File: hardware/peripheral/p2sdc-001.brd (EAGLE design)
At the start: 91 x 90 mm, 72 parts, among them IC1 74LS06N, IC2 4066N, J1 MKR, J10 1-Wire, J2 GPIO, J3 Vcc, J4** RLY2, J5 SPI, J6 LED, J7 DIN5, J8 DIN5, J9 DIN5, K1 G5V1, Q1 220mA/50V/3.5Ω, Q2 220mA/50V/3.5Ω, T1 2SC1815, U1 DS18B20

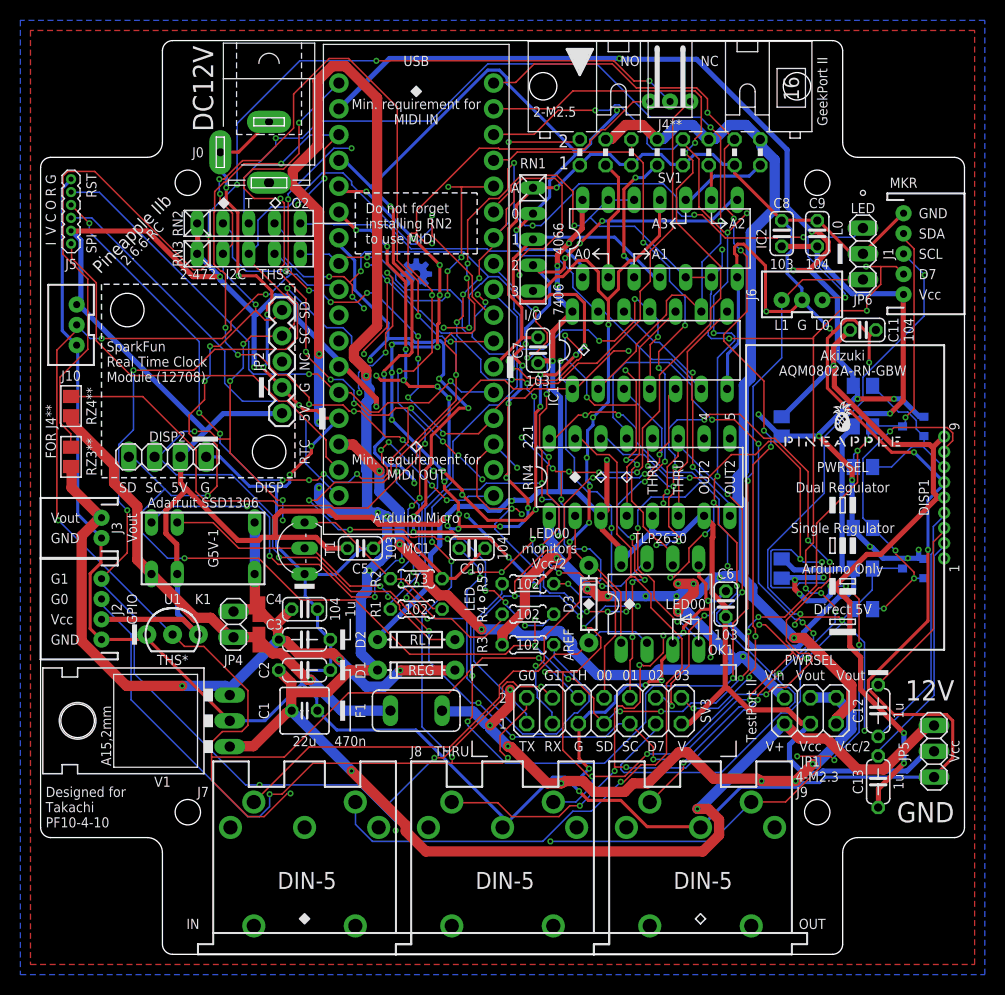
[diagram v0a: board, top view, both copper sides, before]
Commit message: Removed parts.
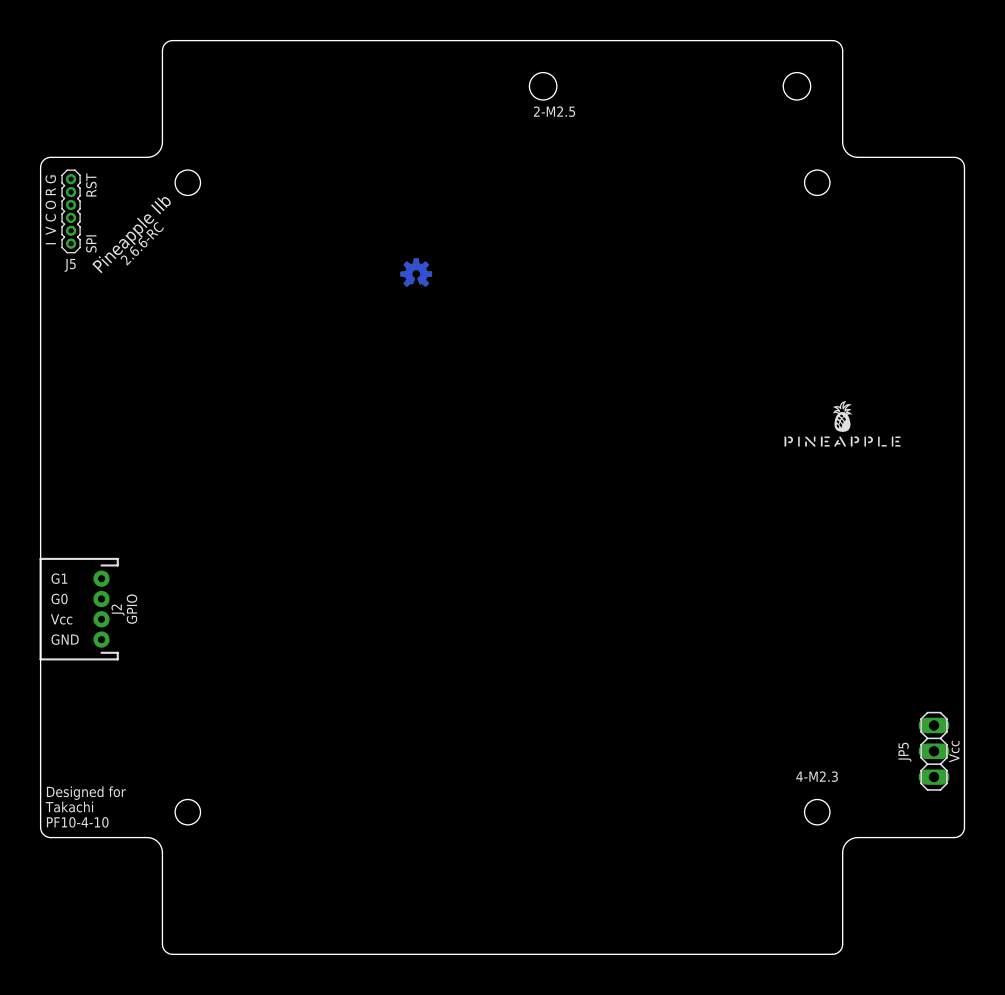
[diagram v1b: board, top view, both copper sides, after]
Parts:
- removed A, B: (no value), wirepad:SMD1,27-2,54
- removed C1: 22u, rcl:C025-050X050
- removed C10, C11, C4: 100n, rcl:C025-024X044
- removed C12, C13, C3: 1u, rcl:C050-024X044
- removed C2: 470n, rcl:C050-024X044
- removed C5, C6, C7, C8: 10n, resistor:C025-024X044
- removed C9: 100n, resistor:C025-024X044
- removed D1, D2, D3: (no value), SparkFun-DiscreteSemi:DIODE-1N4148
- removed DISP1: AQM0802A-RN-GBW, AQM0802A-RN-GBW:AQM0802A-RN-GBW-FOOTPRINT
- removed DISP2: MNTR, pinhead:1X04
- removed F1: 1.8A, fuse:TE5
- removed H1, H2: STAND-OFF, SparkFun-Hardware:STAND-OFF
- removed IC1: 74LS06N, 74xx-us:DIL14
- removed IC2: 4066N, 40xx:DIL14
- removed J0: (no value), con-jack:SPC4077
- removed J1: MKR, SparkFun-Connectors:JST-5-PTH
- removed J10: 1-Wire, SparkFun-Connectors:JST-3-PTH-VERT
- removed J3: Vcc, SparkFun-Connectors:JST-2-PTH
- removed J4**: RLY2, SparkFun-Connectors:JST-3-PTH-NS
- removed J6: LED, SparkFun-Connectors:JST-3-PTH-VERT
- removed J7, J8, J9: DIN5, SparkFun-Connectors:DIN5-RA-PTH
- removed JP1: PWRSEL, pinhead:2X03
- removed JP2: RTC, SparkFun-Connectors:1X05
- removed JP4: RLYJMP, pinhead:1X02
- removed JP6: LED, pinhead:1X03
- removed K1: G5V1, relay:G5V1
- removed MC1: ARDUINOMICRO, adafruit:ARDUINOMICRO
- removed OK1: HCPL2630, optocoupler:DIL08
- removed Q1, Q2: 220mA/50V/3.5Ω, SparkFun-DiscreteSemi:SOT23-3
- removed R1, R3, R4, R5: 1k, resistor:0204/5
- removed R101, R102, R103, R104: 10k, rcl:M2012
- removed R2: 47k, resistor:0204/5
- removed RN1: 10k, resistor-net:RN-5
- removed RN2, RN3: 4.7k, resistor-net:RN-5
- removed RN4: 220, resistor-dil:DIL16
- removed RZ1***, RZ2***, RZ3**, RZ4**, VCCBRIDGE***: Inf, rcl:M2012
- removed SV1: (no value), con-ml:ML16L
- removed SV3: Testport II, pinhead:2X07
- removed T1: 2SC1815, transistor:TO92-ECB
- removed U1: DS18B20, SparkFun-Sensors:TO-92-AMMO
- removed V1: 5V, v-reg:78XXL
- removed VDDBRIDGE: 0, rcl:M2012
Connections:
- removed net ANLG0: IC2.1, MC1.P$31, RN1.2
- removed net ANLG0R: IC2.2, SV1.3
- removed net ANLG1: IC2.4, MC1.P$30, RN1.3
- removed net ANLG1R: IC2.3, SV1.7
- removed net ANLG2: IC2.8, MC1.P$29, RN1.4
- removed net ANLG2R: IC2.9, SV1.11
- removed net ANLG3: IC2.11, MC1.P$28, RN1.5
- removed net ANLG3R: IC2.10, SV1.15
- removed net AREF: C10.1, MC1.P$32, R3.1
- removed net CAP1N: C12.2, DISP1.3
- removed net CAP1P: C12.1, DISP1.4
- removed net D7GATE: IC2.12, IC2.13, IC2.5, IC2.6, J1.4, MC1.P$6, SV3.11
- removed net DTCT0: MC1.P$7, SV1.2, SV3.8
- removed net DTCT1: MC1.P$4, SV1.6, SV3.10
- removed net DTCT2: MC1.P$3, SV1.10, SV3.12
- removed net DTCT3: MC1.P$1, SV1.14, SV3.14
- removed net LCDVOUT: C13.2, DISP1.2
- removed net LED0: MC1.P$34, R4.2
- removed net LED0A: J6.3, JP6.3, R4.1
- removed net LED1: MC1.P$2, R5.2
- removed net LED1A: J6.1, JP6.1, R5.1
- removed net MIDIINSND: D3.C, OK1.1, RN4.2
- removed net MIRTN: D3.A, J7.5, OK1.2
- removed net MISND: J7.4, RN4.15
- removed net MNTR: MC1.P$27, OK1.6, RN3.5
- removed net MNTRA: OK1.4, RN4.16
- removed net MO2RTN: RN4.9
- removed net MO2RTNRAW: IC1.12, RN4.8
- removed net MO2SND: RN4.10
- removed net MORTN: J9.5, RN4.13
- removed net MORTNRAW: IC1.10, RN4.4
- removed net MOSND: J9.4, RN4.14
- removed net MTRTN: J8.5, RN4.11
- removed net MTRTNRAW: IC1.8, RN4.6
- removed net MTSND: J8.4, RN4.12
- removed net NMO2RTN: IC1.13, IC1.6, RN2.5
- removed net NMORTN: IC1.11, IC1.4, RN2.4
- removed net NMTRTN: IC1.2, IC1.9, RN2.3
- removed net RLY: MC1.P$9, R1.2
- removed net RLYDRV: R1.1, R2.2, T1.B
- removed net RLYOUT: J4**.1, K1.10
- removed net RLYOUT1: J4**.2, RZ3**.2
- removed net RLYOUT2: J4**.3, RZ4**.2
- removed net RLYSNK: D2.A, K1.9, T1.C
- removed net RX: IC1.1, MC1.P$14, OK1.7, RN2.2, SV3.3
- removed net SCL: DISP2.3, J1.3, JP2.4, MC1.P$10, Q1.3, R101.1, RN3.3, RZ1***.1, SV3.9
- removed net SCL3V: DISP1.8, Q1.2, R102.1, RZ1***.2
- removed net SDA: DISP2.4, J1.2, JP2.5, MC1.P$11, Q2.3, R103.1, RN3.2, RZ2***.1, SV3.7
- removed net SDA3V: DISP1.7, Q2.2, R104.1, RZ2***.2
- removed net THS: J10.2, MC1.P$26, RN3.4, SV3.6, U1.2
- removed net TX: IC1.3, IC1.5, MC1.P$15, SV3.1
- removed net VCC/2: JP1.5, R3.2, RN4.1, SV1.12, SV1.16, SV1.4, SV1.8
- removed net VCC/VDD: C11.1, C13.1, DISP1.5, DISP1.9, VCCBRIDGE***.1, VDDBRIDGE.1
- removed net VDD: MC1.P$33, Q1.1, Q2.1, R102.2, R104.2, VDDBRIDGE.2
- removed net VIN: JP1.2, MC1.P$20
- removed net VOUT: F1.2, JP1.4, JP1.6
- removed net VOUTRAW: B.1, C3.1, C4.1, D1.A, J3.2, JP4.2, K1.5, K1.6, RZ3**.1, V1.OUT
- removed net VOUTRAW2: A.1, F1.1, JP4.1, K1.1, RZ4**.1
- net GND: no longer C1.2, C10.2, C11.2, C2.2, C3.2, C4.2, C5.2, C6.2, C7.2, C8.2, C9.2, DISP1.6, DISP2.1, IC1.7, IC2.7, J0.1, J0.2, J1.1, J10.1, J3.1, J6.2, J8.2, J9.2, JP2.2, JP6.2, MC1.P$12, MC1.P$21, OK1.3, OK1.5, R2.1, RN1.1, SV1.1, SV1.13, SV1.5, SV1.9, SV3.5, T1.E, U1.1, V1.GND
- net GPIO0: no longer MC1.P$8, SV3.2
- net GPIO1: no longer MC1.P$5, SV3.4
- net MISO: no longer MC1.P$19
- net MOSI: no longer MC1.P$17
- net RST: no longer MC1.P$13, MC1.P$22
- net SCK: no longer MC1.P$18
- net V+: no longer C1.1, C2.1, D1.C, J0.3, JP1.1, V1.IN
- net VCC: no longer C5.1, C6.1, C7.1, C8.1, C9.1, D2.C, DISP2.2, IC1.14, IC2.14, J1.5, J10.3, JP1.3, JP2.1, K1.2, MC1.P$23, OK1.8, R101.2, R103.2, RN2.1, RN3.1, RN4.3, RN4.5, RN4.7, SV3.13, U1.3, VCCBRIDGE***.2
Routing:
- net GND: track 470.3 -> 0.00 mm, vias 20 -> 0
- net VCC: track 373.2 -> 0.00 mm, vias 11 -> 0
- net SCL: track 252.2 -> 0.00 mm, vias 19 -> 0
- net SDA: track 242.7 -> 0.00 mm, vias 20 -> 0
- net V+: track 218.5 -> 0.00 mm, vias 9 -> 0
- net GPIO1: track 160.7 -> 0.00 mm, vias 14 -> 0
- net LED0A: track 143.3 -> 0.00 mm, vias 13 -> 0
- net THS: track 142.2 -> 0.00 mm, vias 5 -> 0
- net GPIO0: track 138.0 -> 0.00 mm, vias 11 -> 0
- net D7GATE: track 136.1 -> 0.00 mm, vias 8 -> 0
- net RX: track 124.9 -> 0.00 mm, vias 15 -> 0
- net AREF: track 122.8 -> 0.00 mm, vias 14 -> 0
- net VDD: track 121.5 -> 0.00 mm, vias 11 -> 0
- net VCC/2: track 120.6 -> 0.00 mm, vias 7 -> 0
- net MTSND: track 119.6 -> 0.00 mm, vias 14 -> 0
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- removed copper zone on layer 1, net GND
- removed copper zone on layer 16, net GND
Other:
- board text removed: "0"
- board text removed: "00"
- board text removed: "01"
- board text removed: "02"
- board text removed: "03"
- board text removed: "1"
- board text removed: "102"
- board text removed: "103"
- board text removed: "104"
- board text removed: "12V"
- board text removed: "1u"
- board text removed: "2"
- board text removed: "2-472"
- board text removed: "2-BSS138"
- board text removed: "221"
- board text removed: "22u"
- board text removed: "3"
- board text removed: "3.3V I2C"
- board text removed: "4"
- board text removed: "4-103"
- board text removed: "4066"
- board text removed: "470n"
- board text removed: "473"
- board text removed: "5"
- board text removed: "5V"
- board text removed: "5V I2C***"
- board text removed: "7406"
- board text removed: "9"
- board text removed: "A"
- board text removed: "A0"
- board text removed: "A1"
- board text removed: "A2"
- board text removed: "A3"
- board text removed: "AREF"
- board text removed: "Adafruit SSD1306"
- board text removed: "Akizuki AQM0802A-RN-GBW"
- board text removed: "Arduino Micro"
- board text removed: "Arduino Only"
- board text removed: "C."
- board text removed: "D7"
- board text removed: "DC12V"
- board text removed: "DISP"
- board text removed: "Direct 5V"
- board text removed: "Do not forget installing RN2 to use MIDI"
- board text removed: "Dual Regulator"
- board text removed: "FOR J4**"
- board text removed: "G5V-1"
- board text removed: "GeekPort II"
- board text removed: "I/O"
- board text removed: "I2C"
- board text removed: "I2C/THS*/MNTR"
- board text removed: "IN"
- board text removed: "L0"
- board text removed: "L1"
- board text removed: "LED"
- board text removed: "LED00"
- board text removed: "LED00 monitors Vcc/2"
- board text removed: "MC1"
- board text removed: "MIDI"
- board text removed: "MIDI IN"
- board text removed: "MIDI OUT"
- board text removed: "MKR"
- board text removed: "Min. requirement for MIDI IN"
- board text removed: "Min. requirement for MIDI OUT"
- board text removed: "N.C."
- board text removed: "N.O."
- board text removed: "NC"
- board text removed: "NO"
- board text removed: "O2"
- board text removed: "OUT"
- board text removed: "OUT2"
- board text removed: "PWR"
- board text removed: "PWRSEL"
- board text removed: "REG"
- board text removed: "RLY"
- board text removed: "RTC"
- board text removed: "RX"
- board text removed: "Relay-Common"
- board text removed: "Relay-N.C."
- board text removed: "Relay-N.O."
- board text removed: "SC"
- board text removed: "SCL"
- board text removed: "SD"
- board text removed: "SDA"
- board text removed: "Single Regulator"
- board text removed: "SparkFun Real Time Clock Module (12708)"
- board text removed: "T"
- board text removed: "TH"
- board text removed: "THRU"
- board text removed: "THS*"
- board text removed: "TLP2630"
- board text removed: "TX"
- board text removed: "TestPort II"
- board text removed: "USB"
- board text removed: "V+"
- board text removed: "V/2"
- board text removed: "Vcc/2"
- board text removed: "Vdd"
- board text removed: "Vin"
- board text removed: "Vo"
- board text removed: "Vout"

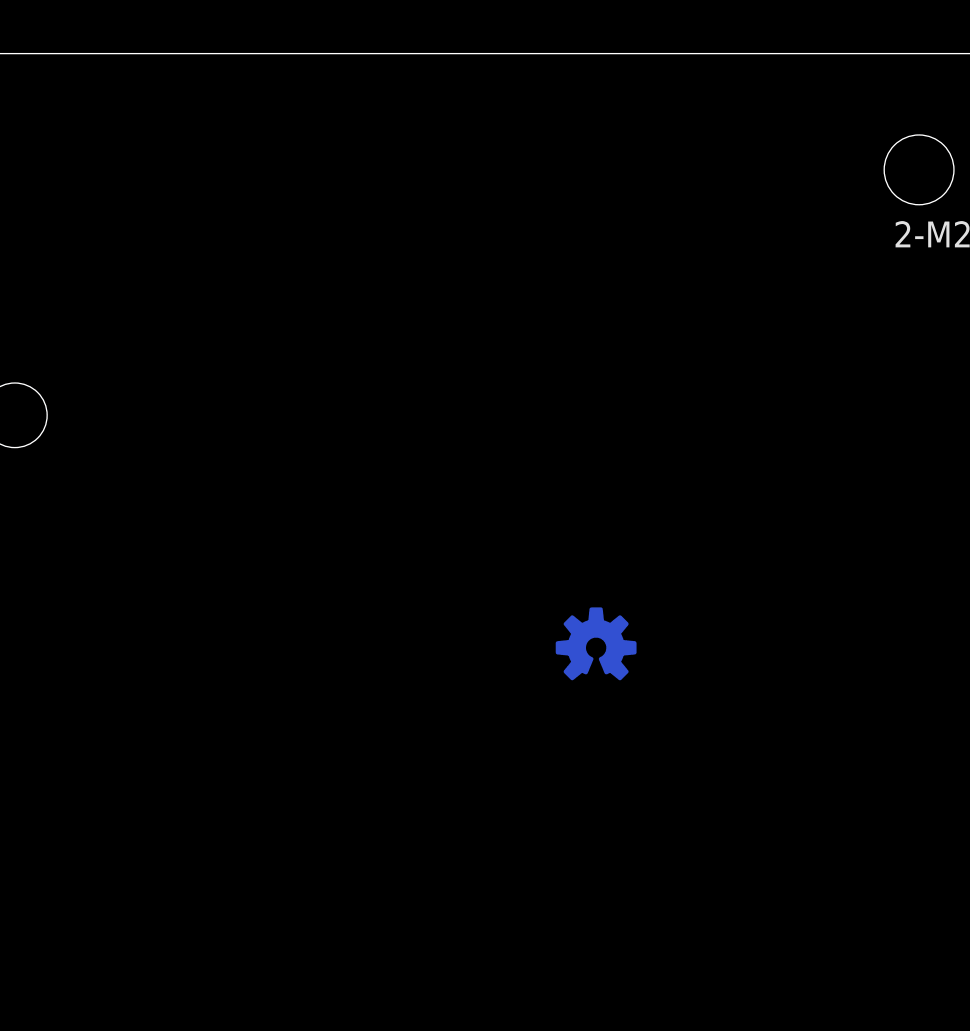
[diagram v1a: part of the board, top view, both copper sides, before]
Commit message: Positioning of the breakout card.
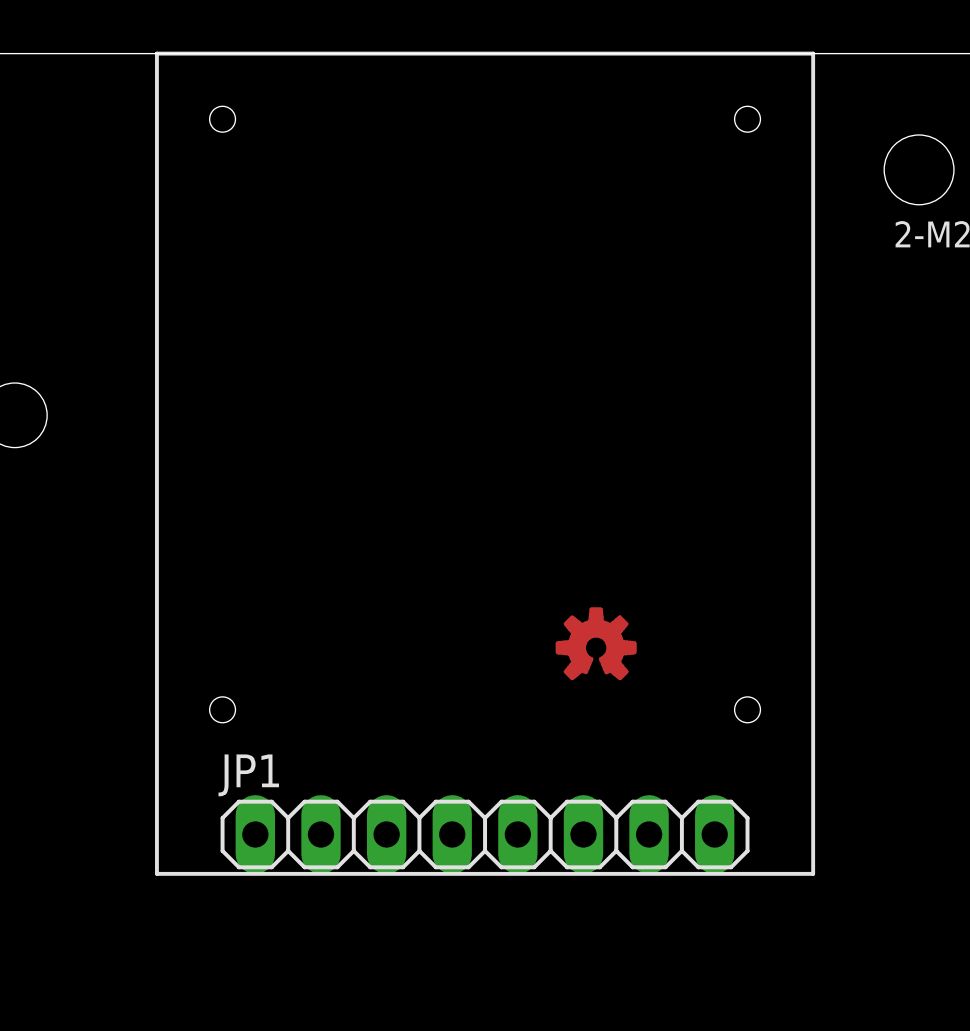
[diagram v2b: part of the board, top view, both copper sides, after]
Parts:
- added JP1: (no value), pinhead:1X08
- flipped LOGO1 to the top
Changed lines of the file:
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@@
 <setting verticaltext="up"/>
 </settings>
-<grid distance="0.5" unitdist="mm" unit="mm" style="lines" multiple="2" display="yes" altdistance="50" altunitdist="mil" altunit="mil"/>
+<grid distance="1" unitdist="mm" unit="mm" style="lines" multiple="1" display="yes" altdistance="50" altunitdist="mil" altunit="mil"/>
 <layers>
 <layer number="1" name="Top" color="4" fill="1" visible="yes" active="yes"/>
@@
 <layer number="21" name="tPlace" color="7" fill="1" visible="yes" active="yes"/>
 <layer number="22" name="bPlace" color="7" fill="1" visible="yes" active="yes"/>
-<layer number="23" name="tOrigins" color="15" fill="1" visible="no" active="yes"/>
-<layer number="24" name="bOrigins" color="15" fill="1" visible="no" active="yes"/>
+<layer number="23" name="tOrigins" color="15" fill="1" visible="yes" active="yes"/>
+<layer number="24" name="bOrigins" color="15" fill="1" visible="yes" active="yes"/>
 <layer number="25" name="tNames" color="7" fill="1" visible="yes" active="yes"/>
 <layer number="26" name="bNames" color="7" fill="1" visible="yes" active="yes"/>
@@
 <text x="5" y="75.715" size="1" layer="25" rot="R90" align="center">RST</text>
 <text x="1.5" y="73.175" size="1" layer="26" rot="MR90" align="center">SPI</text>
+<wire x1="20" y1="90" x2="45.4" y2="90" width="0.15" layer="21"/>
+<wire x1="45.4" y1="90" x2="45.4" y2="58.25" width="0.15" layer="21"/>
+<wire x1="45.4" y1="58.25" x2="20" y2="58.25" width="0.15" layer="21"/>
+<wire x1="20" y1="58.25" x2="20" y2="90" width="0.15" layer="21"/>
+<hole x="22.54" y="87.46" drill="1"/>
+<hole x="42.86" y="87.46" drill="1"/>
+<hole x="22.54" y="64.6" drill="1"/>
+<hole x="42.86" y="64.6" drill="1"/>
 </plain>
 <attributes>
@@
 </autorouter>
 <elements>
-<element name="LOGO1" library="SparkFun-Aesthetics" package="OSHW-LOGO-S_COPPER" value="OSHW-LOGOS-COPPER" x="37" y="67" smashed="yes" rot="MR0"/>
+<element name="LOGO1" library="SparkFun-Aesthetics" package="OSHW-LOGO-S_COPPER" value="OSHW-LOGOS-COPPER" x="37" y="67" smashed="yes"/>
 <element name="U$1" library="pineapple" package="PINEAPPLE450_SILK" value="PINEAPPLE450_SILK" x="79" y="50" smashed="yes"/>
 <element name="JP5" library="pinhead" library_urn="urn:adsk.eagle:library:325" package="1X03" package3d_urn="urn:adsk.eagle:package:22458/2" value="PWR" x="88" y="20" smashed="yes" rot="R90">
@@
 <attribute name="VALUE" x="4.651" y="69.619" size="0.6096" layer="27" font="vector" ratio="20" rot="R90"/>
 </element>
+<element name="JP1" library="pinhead" library_urn="urn:adsk.eagle:library:325" package="1X08" package3d_urn="urn:adsk.eagle:package:22409/2" value="" x="32.7" y="59.774" smashed="yes">
+<attribute name="NAME" x="22.4638" y="61.6028" size="1.27" layer="25" ratio="10"/>
+<attribute name="POPULARITY" value="67" x="32.7" y="59.774" size="1.778" layer="27" display="off"/>
+<attribute name="VALUE" x="22.54" y="56.599" size="1.27" layer="27"/>
+</element>
 </elements>
